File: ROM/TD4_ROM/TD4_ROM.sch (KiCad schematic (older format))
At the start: 2 parts

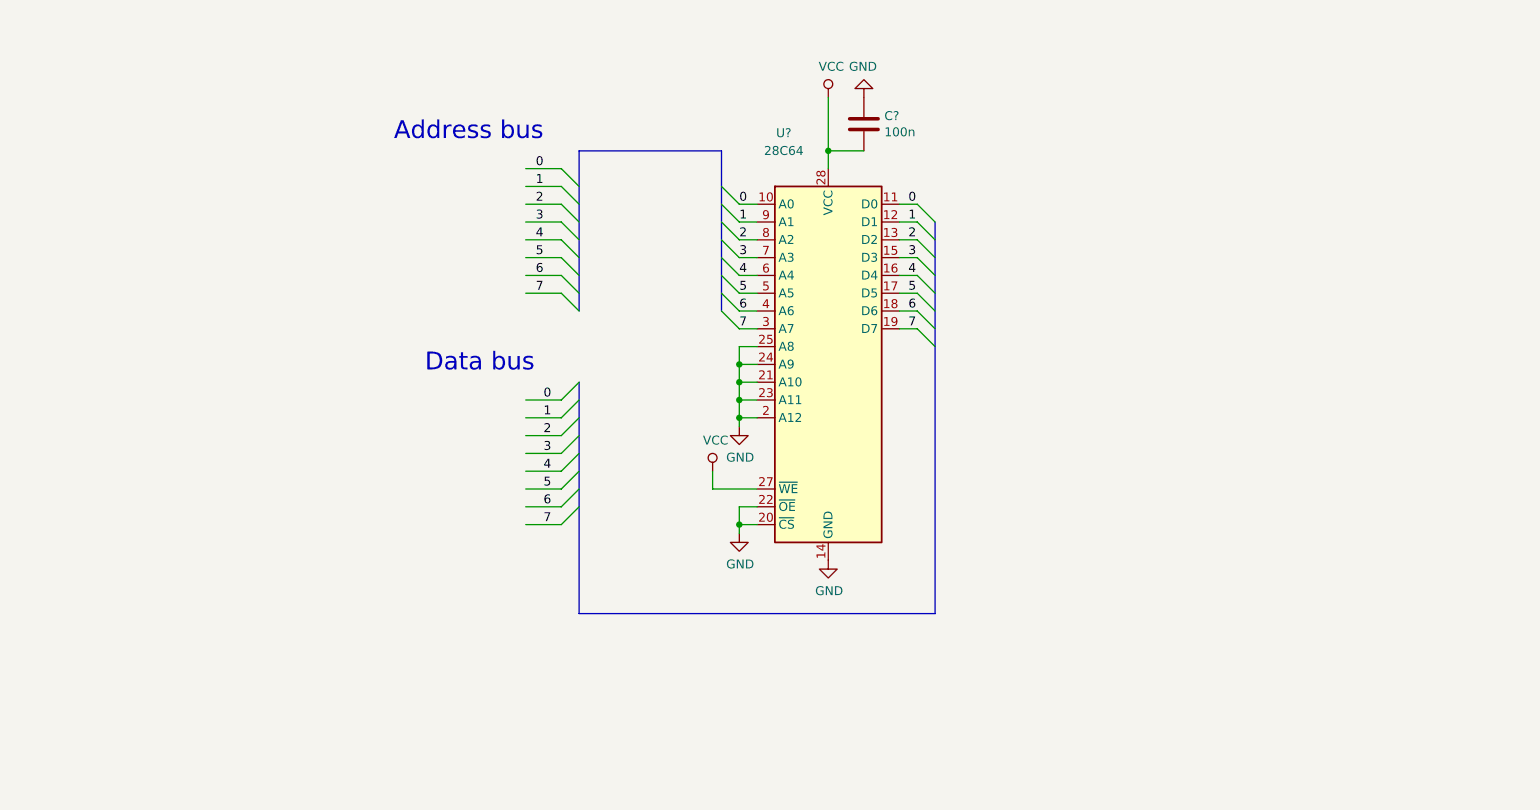
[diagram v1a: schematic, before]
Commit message: ROM refactoring done
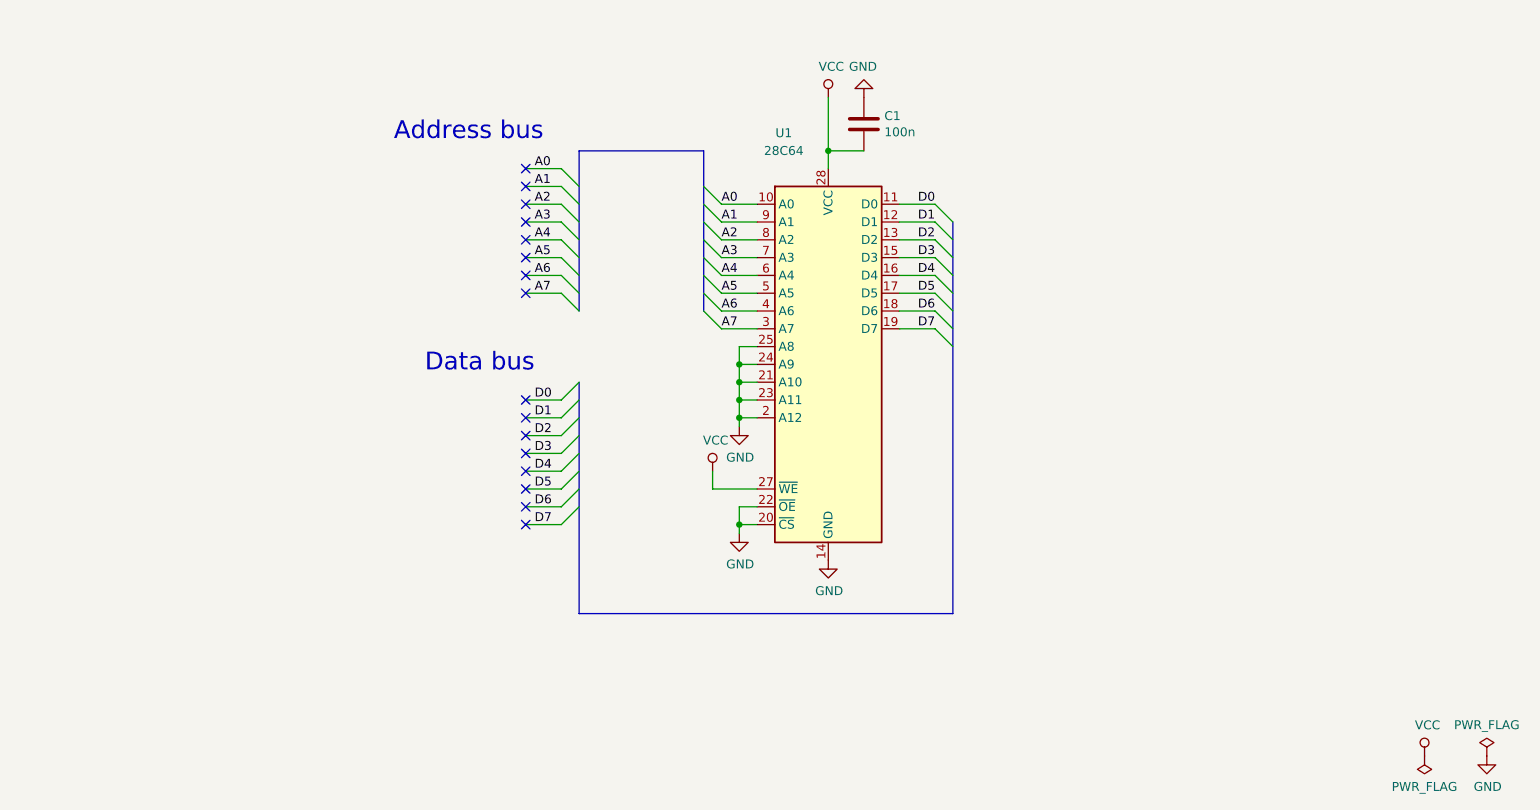
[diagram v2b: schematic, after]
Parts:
- gave numbers to parts that had none: 2
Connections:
- net labels added: A0, A1, A2, A3, A4, A5, A6, A7, D0, D1, D2, D3, D4, D5, D6, D7
- net labels removed: 0, 1, 2, 3, 4, 5, 6, 7
- no-connect marks 0 -> 16

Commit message: Added backplane connectors to all PCBs
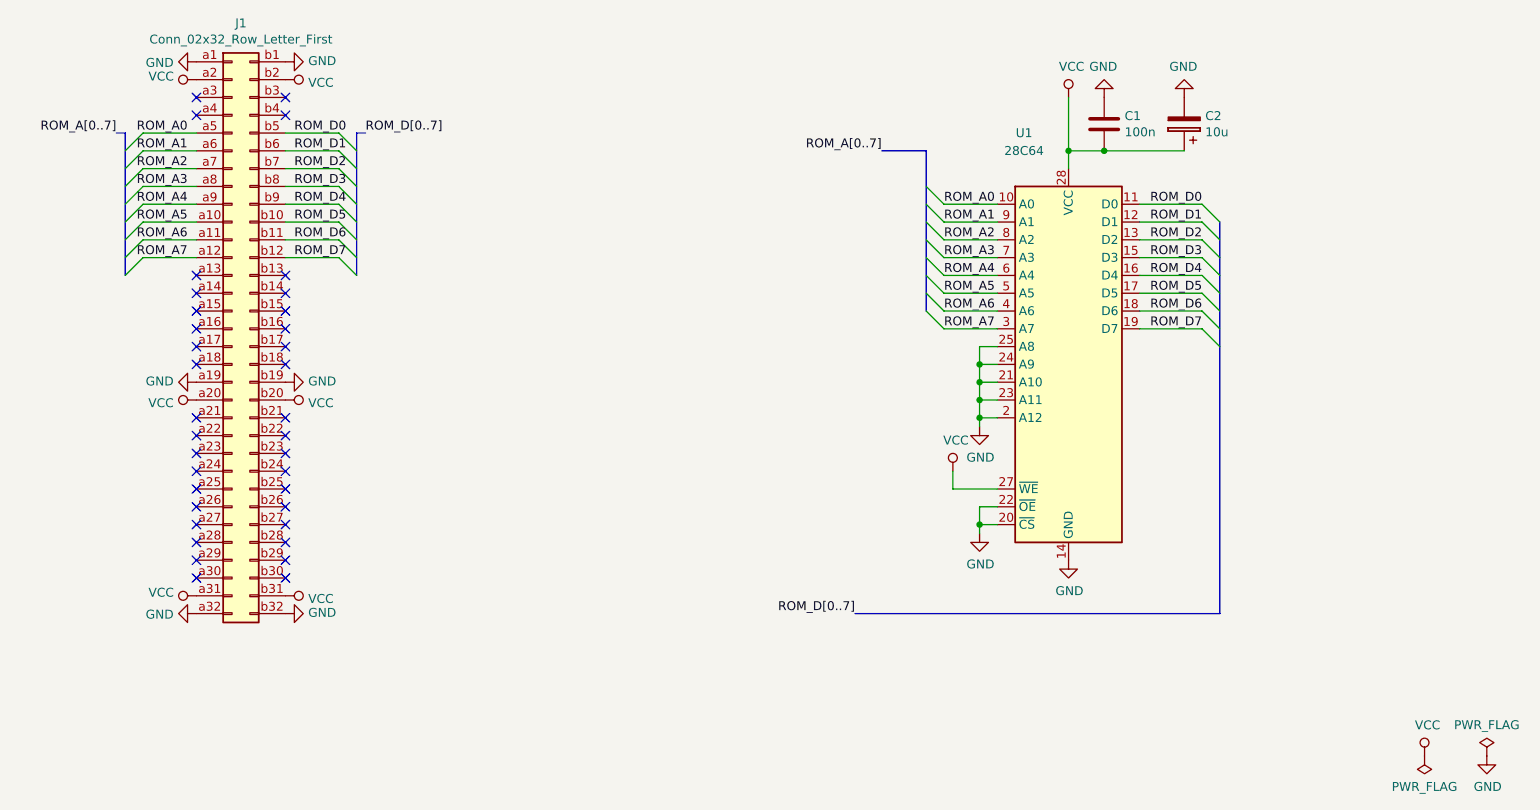
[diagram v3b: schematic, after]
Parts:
- added C2: 10u, Capacitor_Tantalum_SMD:CP_EIA-3216-18_Kemet-A, symbol Device:CP
- added J1: Conn_02x32_Row_Letter_First, Connector_DIN:DIN41612_B_2x32_Horizontal, symbol Connector_Generic:Conn_02x32_Row_Letter_First
- C1: footprint (none) -> Capacitor_SMD:C_0805_2012Metric
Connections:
- net GND: now also C2.2, J1.a1 (Pin_a1), J1.a19 (Pin_a19), J1.a32 (Pin_a32), J1.b1 (Pin_b1), J1.b19 (Pin_b19), J1.b32 (Pin_b32)
- net VCC: now also C2.1, J1.a2 (Pin_a2), J1.a20 (Pin_a20), J1.a31 (Pin_a31), J1.b2 (Pin_b2), J1.b20 (Pin_b20), J1.b31 (Pin_b31)
- net A0 renamed ROM_A0
- net ROM_A0: now also J1.a5 (Pin_a5)
- net A1 renamed ROM_A1
- net ROM_A1: now also J1.a6 (Pin_a6)
- net A2 renamed ROM_A2
- net ROM_A2: now also J1.a7 (Pin_a7)
- net A3 renamed ROM_A3
- net ROM_A3: now also J1.a8 (Pin_a8)
- net A4 renamed ROM_A4
- net ROM_A4: now also J1.a9 (Pin_a9)
- net A5 renamed ROM_A5
- net ROM_A5: now also J1.a10 (Pin_a10)
- net A6 renamed ROM_A6
- net ROM_A6: now also J1.a11 (Pin_a11)
- net A7 renamed ROM_A7
- net ROM_A7: now also J1.a12 (Pin_a12)
- net D0 renamed ROM_D0
- net ROM_D0: now also J1.b5 (Pin_b5)
- net D1 renamed ROM_D1
- net ROM_D1: now also J1.b6 (Pin_b6)
- net D2 renamed ROM_D2
- net ROM_D2: now also J1.b7 (Pin_b7)
- net D3 renamed ROM_D3
- net ROM_D3: now also J1.b8 (Pin_b8)
- net D4 renamed ROM_D4
- net ROM_D4: now also J1.b9 (Pin_b9)
- net D5 renamed ROM_D5
- net ROM_D5: now also J1.b10 (Pin_b10)
- net D6 renamed ROM_D6
- net ROM_D6: now also J1.b11 (Pin_b11)
- net D7 renamed ROM_D7
- net ROM_D7: now also J1.b12 (Pin_b12)
- no-connect marks 16 -> 36
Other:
- note removed: "Address bus"
- note removed: "Data bus"
- moved on the sheet: C1, U1
